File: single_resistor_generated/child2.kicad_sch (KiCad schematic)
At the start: 1 part

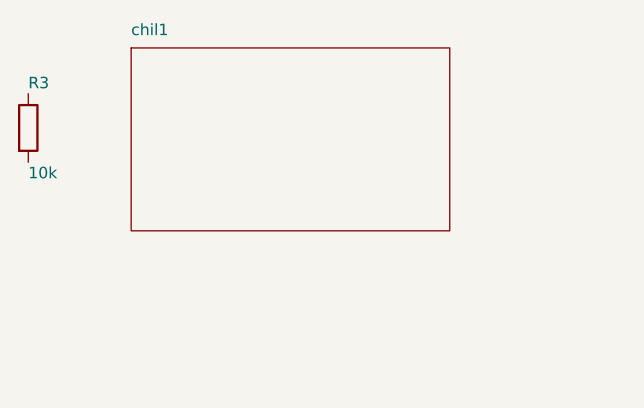
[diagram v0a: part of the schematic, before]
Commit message: adding updated testing code
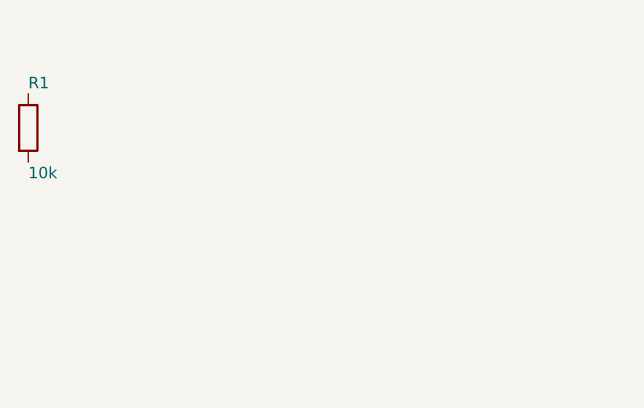
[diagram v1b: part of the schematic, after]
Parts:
- removed R3: 10k, Resistor_SMD:R_0603_1608Metric, symbol Device:R
- added R1: 10k, Resistor_SMD:R_0603_1608Metric, symbol Device:R
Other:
- removed sheet chil1
- title: singe_resistor_generated -> child2
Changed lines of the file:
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@@
 	(paper "A4")
 	(title_block
-		(title singe_resistor_generated)
+		(title child2)
 		(date 2025-08-04)
 		(company Circuit-Synth)
@@
 		(dnp no)
 		(fields_autoplaced yes)
-		(property "Reference" "R3"
+		(property "Reference" "R1"
 			(at 38.1 40.72 0)
 			(effects
@@
 		(instances
 			(project
-				""
-				(path
-					"/4230698c-b526-4307-9655-afb80e239726"
-					(reference "R3")
-					(unit 1)
-				)
-			)
-		)
-	)
-	(sheet
-		(at 49.53 36.83)
-		(size 35.4 20.32)
-		(stroke
-			(width 0.12)
-			(type solid)
-		)
-		(fill
-			(color
-				0
-				0
-				0
-				0.0
-			)
-		)
-		(property "Sheetname" "chil1"
-			(at 49.53 35.559999999999995 0)
-			(effects
-				(font
-					(size 1.27 1.27)
-				)
-				(justify left bottom)
-			)
-		)
-		(property "Sheetfile" "chil1.kicad_sch"
-			(at 49.53 58.42 0)
-			(effects
-				(font
-					(size 1.27 1.27)
-				)
-				(justify left top)
-				(hide yes)
-			)
-		)
-		(instances
-			(project
 				"single_resistor_generated"
 				(path
-					"/"
-					(page "1")
+					"/4230698c-b526-4307-9655-afb80e239726/5eda4cf9-f3b7-4753-8ff9-af07e14d51ab/8b524237-4053-4f67-8c74-08cc3453a6a1/38af8e3c-47c5-482a-a87e-dba934441f1e"
+					(reference "R1")
+					(unit 1)
 				)
 			)
@@
 	(sheet_instances
 		(path
-			"/4230698c-b526-4307-9655-afb80e239726"
+			"/4230698c-b526-4307-9655-afb80e239726/5eda4cf9-f3b7-4753-8ff9-af07e14d51ab/8b524237-4053-4f67-8c74-08cc3453a6a1/38af8e3c-47c5-482a-a87e-dba934441f1e"
 			(page "1")
 		)
